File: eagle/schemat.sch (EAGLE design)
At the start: 35 parts, among them IC1 MEGA8-AI, Q1 N-MOSFET BSS138, Q2 N-MOSFET BSS138, U1 LCD-16X2SILK, Y1 16MHz

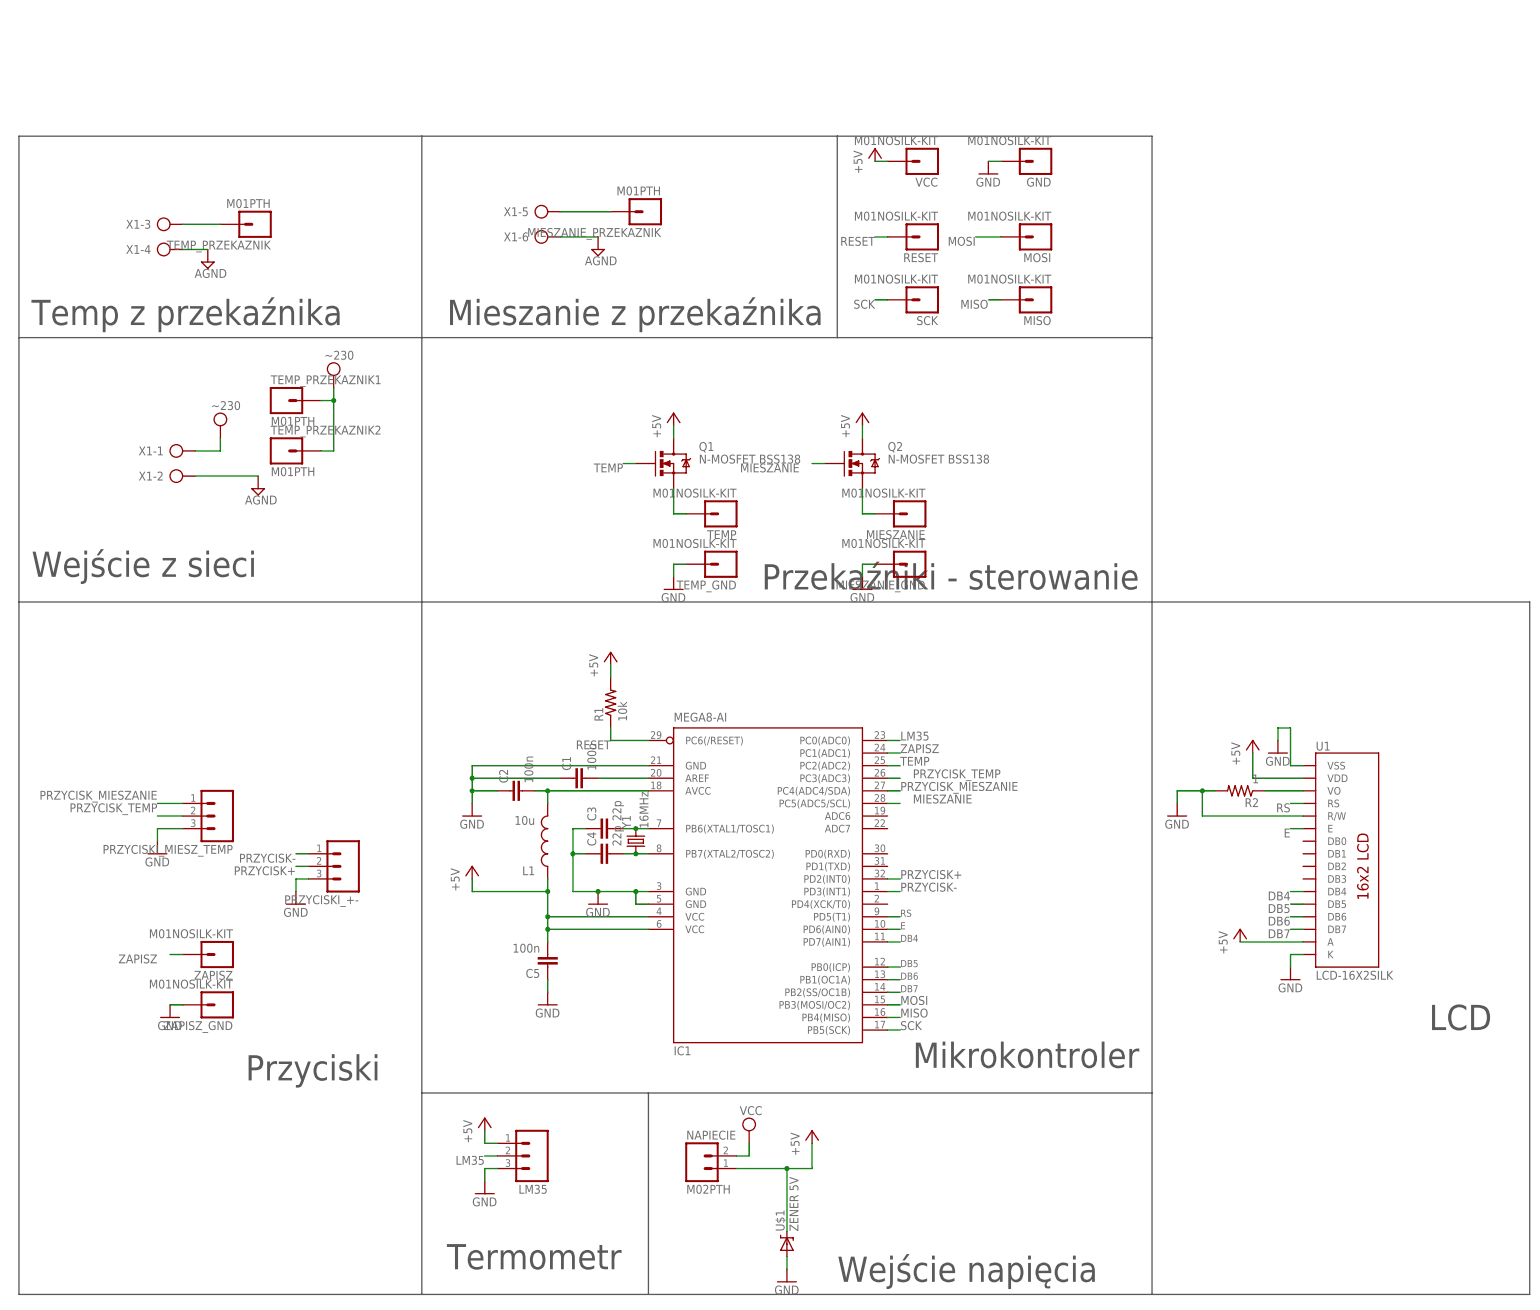
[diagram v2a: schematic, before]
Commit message: Zmieniony schemat + zmiany w programie
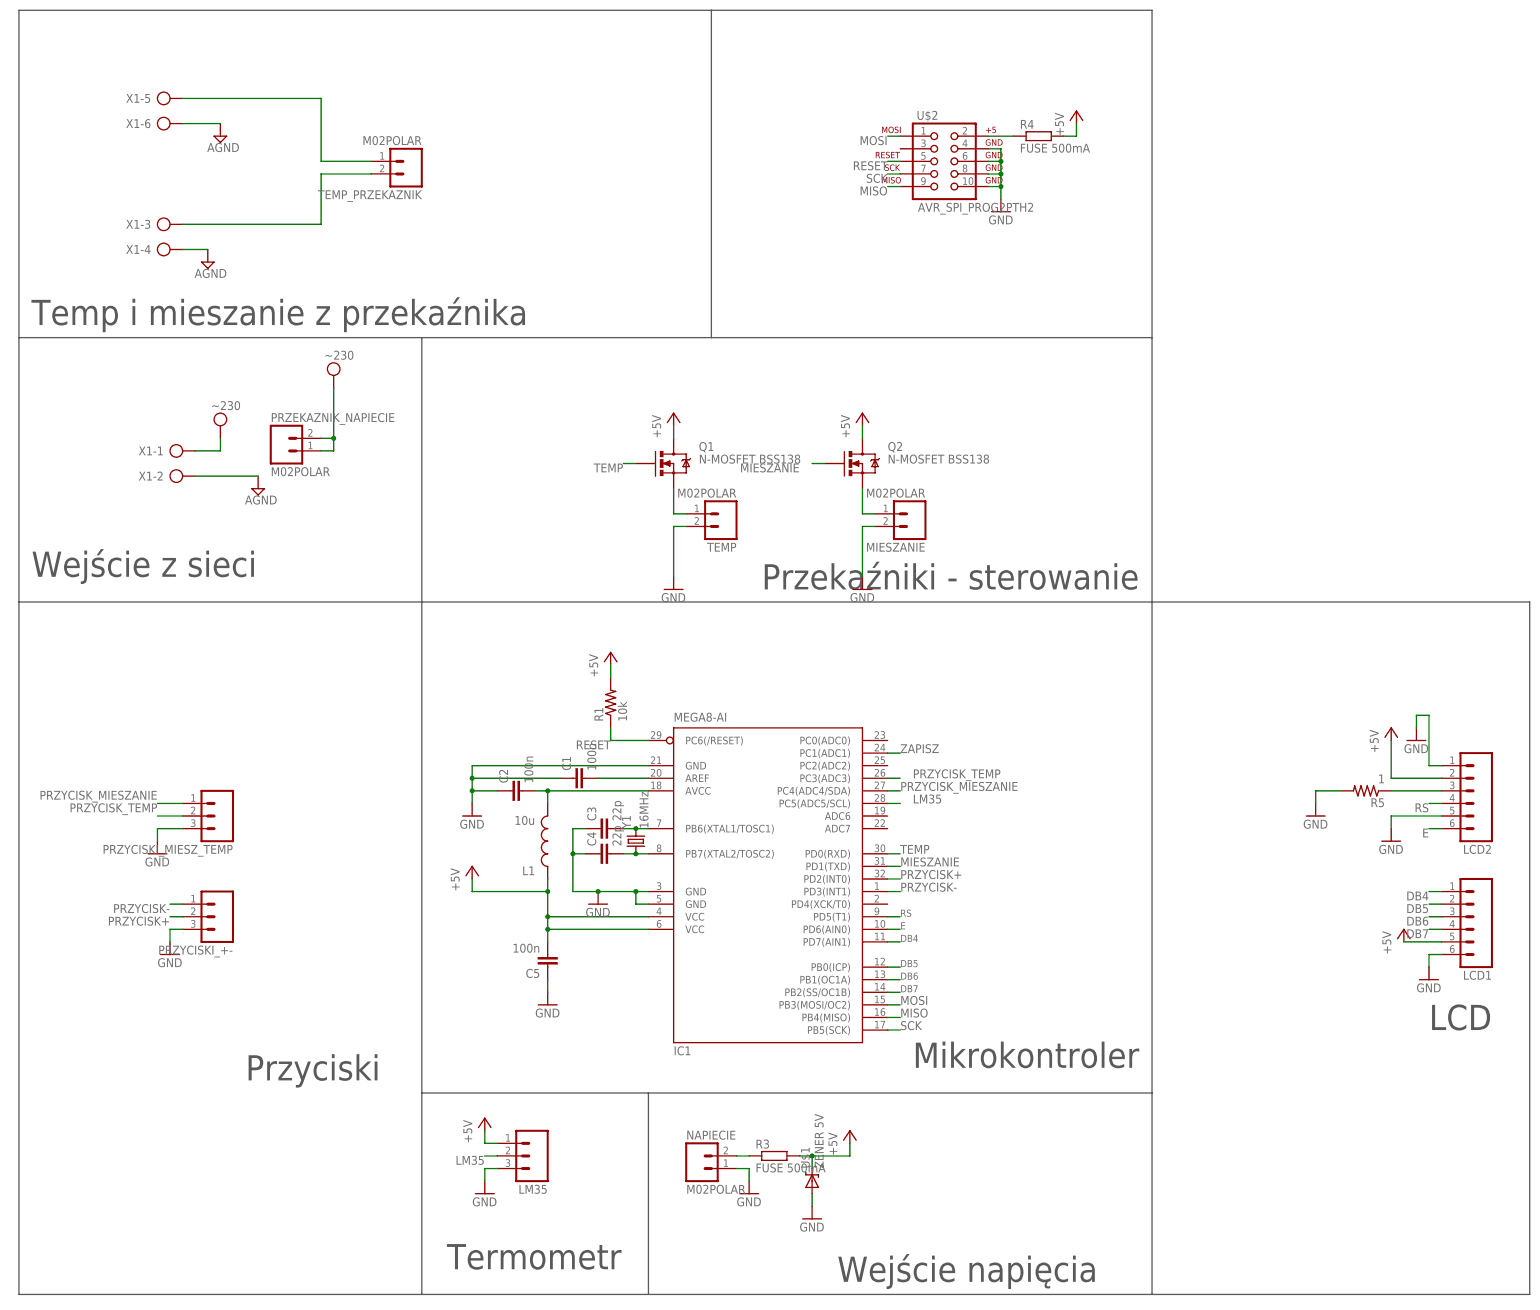
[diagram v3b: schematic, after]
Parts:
- removed GND, MIESZANIE_GND, MISO, MOSI, RESET, SCK, TEMP_GND, VCC, ZAPISZ, ZAPISZ_GND: M01NOSILK-KIT, SparkFun-Connectors:M01NOSILK-KIT
- removed MIESZANIE_PRZEKAZNIK, TEMP_PRZEKAZNIK1, TEMP_PRZEKAZNIK2: M01PTH, SparkFun-Connectors:M01PTH
- removed R2: 1, SparkFun-Passives:RESISTOR0805-RES
- removed U1: LCD-16X2SILK, SparkFun-Displays:LCD-16X2SILK
- added LCD1, LCD2: (no value), SparkFun-Connectors:M06POLAR
- added PRZEKAZNIK_NAPIECIE: M02POLAR, SparkFun-Connectors:M02POLAR
- added R3, R4: FUSE 500mA, resistor:R-EU_M0805
- added R5: 1, SparkFun-Passives:RESISTOR0805-RES
- added U$2: AVR_SPI_PROG2PTH2, SparkFun-Connectors:AVR_SPI_PROG2PTH2
- MIESZANIE, TEMP: value M01NOSILK-KIT -> M02POLAR; device SparkFun-Connectors:M01NOSILK-KIT -> SparkFun-Connectors:M02POLAR
- NAPIECIE: value M02PTH -> M02POLAR; device SparkFun-Connectors:M02PTH -> SparkFun-Connectors:M02POLAR
- PRZYCISKI_+-, PRZYCISKI_MIESZ_TEMP: device SparkFun-Connectors:M03LOCK -> SparkFun-Connectors:M03POLAR
- TEMP_PRZEKAZNIK: value M01PTH -> M02POLAR; device SparkFun-Connectors:M01PTH -> SparkFun-Connectors:M02POLAR
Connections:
- removed net N$13: TEMP_PRZEKAZNIK.1, X1-3.KL
- removed net N$9: R2.1, U1.VO
- removed net VCC: NAPIECIE.2
- new net N$10: TEMP_PRZEKAZNIK.2, X1-3.KL
- new net N$11: R4.1, U$2.2
- new net N$16: LCD2.3, R5.1
- new net N$8: NAPIECIE.2, R3.1
- net +5V: now also LCD1.5, LCD2.2, R3.2, R4.2; no longer NAPIECIE.1, U1.A, U1.VDD, VCC.1
- net DB4: now also LCD1.1; no longer U1.DB4
- net DB5: now also LCD1.2; no longer U1.DB5
- net DB6: now also LCD1.3; no longer U1.DB6
- net DB7: now also LCD1.4; no longer U1.DB7
- net E: now also LCD2.6; no longer U1.E
- net GND: now also LCD1.6, LCD2.1, LCD2.5, MIESZANIE.2, NAPIECIE.1, R5.2, TEMP.2, U$2.10, U$2.4, U$2.6, U$2.8; no longer GND.1, MIESZANIE_GND.1, R2.2, TEMP_GND.1, U1.K, U1.R/W, U1.VSS, ZAPISZ_GND.1
- net LM35: now also IC1.PC5(ADC5/SCL); no longer IC1.PC0(ADC0)
- net MIESZANIE: now also IC1.PD1(TXD); no longer IC1.PC5(ADC5/SCL)
- net MISO: now also U$2.9; no longer MISO.1
- net MOSI: now also U$2.1; no longer MOSI.1
- net N$14: now also TEMP_PRZEKAZNIK.1; no longer MIESZANIE_PRZEKAZNIK.1
- net RESET: now also U$2.5; no longer RESET.1
- net RS: now also LCD2.4; no longer U1.RS
- net SCK: now also U$2.7; no longer SCK.1
- net TEMP: now also IC1.PD0(RXD); no longer IC1.PC2(ADC2)
- net VDD: now also PRZEKAZNIK_NAPIECIE.1, PRZEKAZNIK_NAPIECIE.2; no longer TEMP_PRZEKAZNIK1.1, TEMP_PRZEKAZNIK2.1
- net ZAPISZ: no longer ZAPISZ.1
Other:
- note added: "Temp i mieszanie z przekaźnika"
- note removed: "Mieszanie z przekaźnika"
- note removed: "Temp z przekaźnika"
- moved on the sheet: PRZYCISKI_+-, U$1, X1-5, X1-6
